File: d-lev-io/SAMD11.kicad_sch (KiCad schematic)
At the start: 30 parts, among them J6 PROG_HDR, SW1 SW_Push, SW2 SW_Push, SW3 SW_Push, U3 ATSAMD11D14A-M

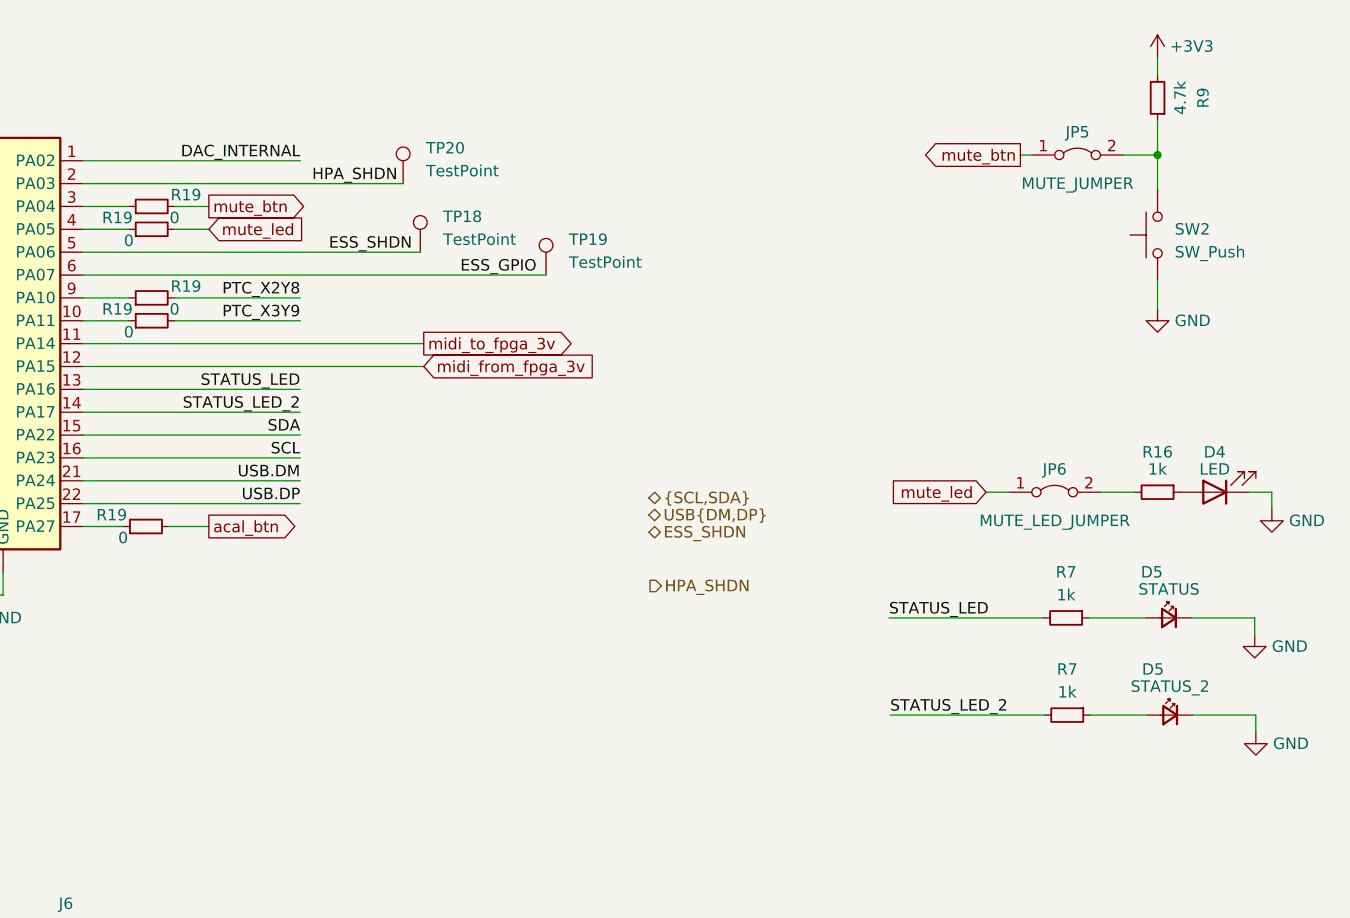
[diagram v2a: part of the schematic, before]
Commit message: io board more analog schematic capture
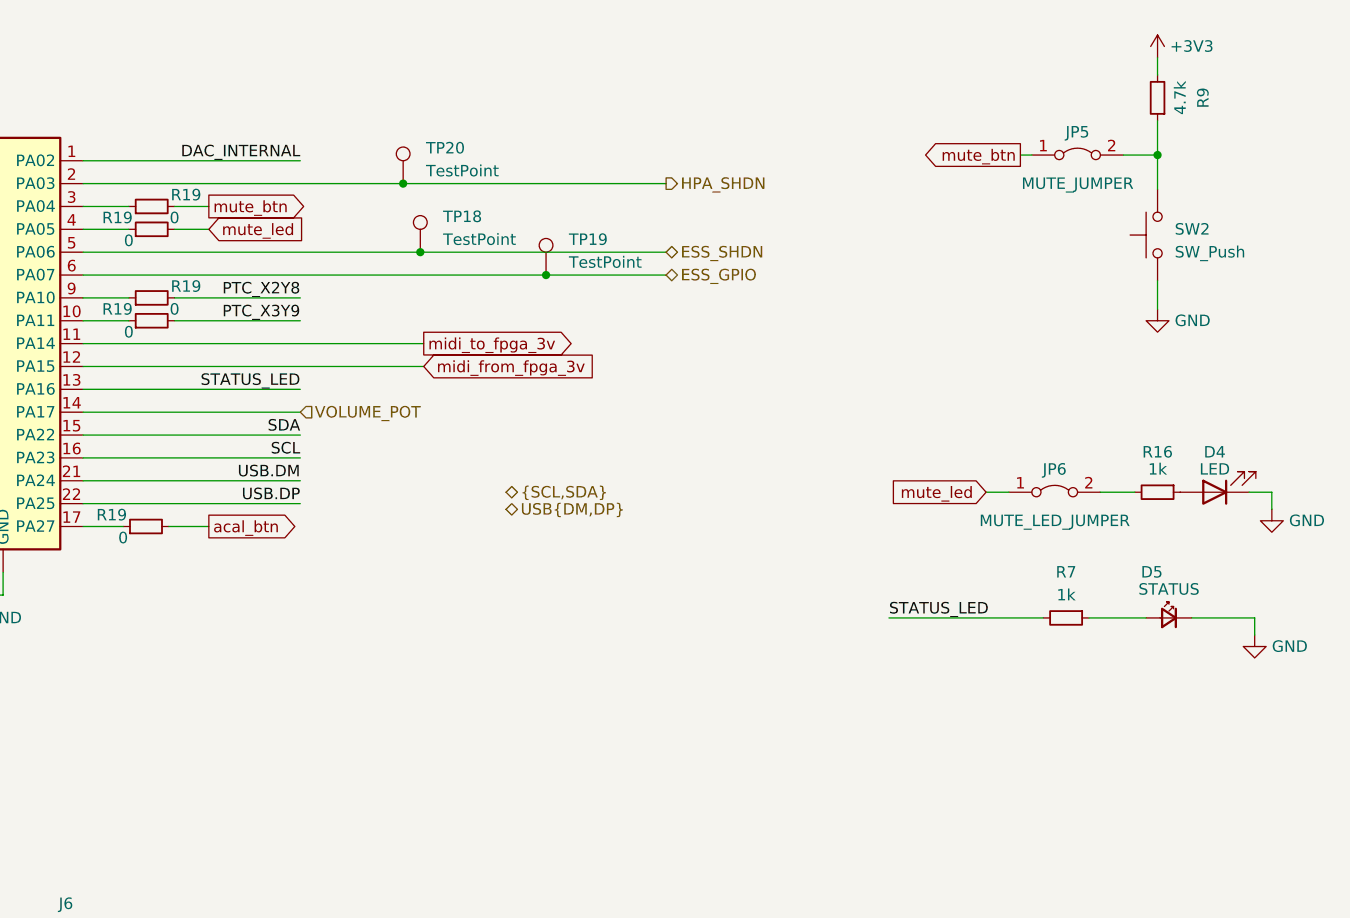
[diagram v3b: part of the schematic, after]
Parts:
- removed D5: STATUS_2, LED_SMD:LED_0603_1608Metric, symbol Device:LED_Small
- removed R7: 1k, Resistor_SMD:R_0603_1608Metric, symbol Device:R_Small
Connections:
- net STATUS_LED_2 renamed VOLUME_POT
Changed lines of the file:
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@@
 (kicad_sch (version 20230121) (generator eeschema)
   (paper "A4")
+  (junction (at 177.8 88.9) (diameter 0) (color 0 0 0 0)
+  )
   (junction (at 261.62 85.725) (diameter 0) (color 0 0 0 0)
   )
@@
   (junction (at 261.62 44.45) (diameter 0) (color 0 0 0 0)
   )
+  (junction (at 179.705 96.52) (diameter 0) (color 0 0 0 0)
+  )
   (junction (at 50.165 153.67) (diameter 0) (color 0 0 0 0)
   )
   (junction (at 49.53 88.9) (diameter 0) (color 0 0 0 0)
+  )
+  (junction (at 193.675 99.06) (diameter 0) (color 0 0 0 0)
   )
   (junction (at 50.165 131.445) (diameter 0) (color 0 0 0 0)
@@
     (stroke (width 0) (type default))
   )
-  (wire (pts (xy 272.542 149.86) (xy 272.542 147.955))
-    (stroke (width 0) (type default))
-  )
   (wire (pts (xy 99.695 89.535) (xy 99.695 88.9))
     (stroke (width 0) (type default))
@@
     (stroke (width 0) (type default))
   )
+  (wire (pts (xy 207.01 96.52) (xy 179.705 96.52))
+    (stroke (width 0) (type default))
+  )
   (wire (pts (xy 47.244 96.52) (xy 47.244 99.06))
     (stroke (width 0) (type default))
@@
     (stroke (width 0) (type default))
   )
-  (wire (pts (xy 231.902 147.955) (xy 249.047 147.955))
-    (stroke (width 0) (type default))
-  )
   (wire (pts (xy 47.244 99.06) (xy 59.69 99.06))
     (stroke (width 0) (type default))
@@
     (stroke (width 0) (type default))
   )
-  (wire (pts (xy 265.557 147.955) (xy 272.542 147.955))
-    (stroke (width 0) (type default))
-  )
   (wire (pts (xy 50.165 139.7) (xy 50.165 140.97))
     (stroke (width 0) (type default))
@@
     (stroke (width 0) (type default))
   )
+  (wire (pts (xy 207.01 99.06) (xy 193.675 99.06))
+    (stroke (width 0) (type default))
+  )
   (wire (pts (xy 61.595 131.445) (xy 61.595 139.065))
     (stroke (width 0) (type default))
@@
     (stroke (width 0) (type default))
   )
+  (wire (pts (xy 177.8 88.9) (xy 207.01 88.9))
+    (stroke (width 0) (type default))
+  )
   (wire (pts (xy 231.775 137.16) (xy 248.92 137.16))
     (stroke (width 0) (type default))
@@
   )
   (wire (pts (xy 142.24 124.46) (xy 166.37 124.46))
-    (stroke (width 0) (type default))
-  )
-  (wire (pts (xy 260.477 147.955) (xy 254.127 147.955))
     (stroke (width 0) (type default))
   )
@@
     (effects (font (size 1.27 1.27)) (justify left bottom))
   )
-  (label "STATUS_LED_2" (at 166.37 114.3 180) (fields_autoplaced)
-    (effects (font (size 1.27 1.27)) (justify right bottom))
-  )
   (label "SCL" (at 166.37 119.38 180) (fields_autoplaced)
     (effects (font (size 1.27 1.27)) (justify right bottom))
@@
     (effects (font (size 1.27 1.27)) (justify right bottom))
   )
-  (label "STATUS_LED_2" (at 231.902 147.955 0) (fields_autoplaced)
-    (effects (font (size 1.27 1.27)) (justify left bottom))
-  )
   (label "SDA" (at 59.69 96.52 180) (fields_autoplaced)
     (effects (font (size 1.27 1.27)) (justify right bottom))
@@
     (effects (font (size 1.27 1.27)) (justify right bottom))
   )
-  (label "ESS_GPIO" (at 184.15 99.06 0) (fields_autoplaced)
-    (effects (font (size 1.27 1.27)) (justify left bottom))
-  )
   (label "STATUS_LED" (at 166.37 111.76 180) (fields_autoplaced)
     (effects (font (size 1.27 1.27)) (justify right bottom))
@@
   )
   (label "DAC_INTERNAL" (at 166.37 86.36 180) (fields_autoplaced)
-    (effects (font (size 1.27 1.27)) (justify right bottom))
-  )
-  (label "ESS_SHDN" (at 169.545 96.52 0) (fields_autoplaced)
-    (effects (font (size 1.27 1.27)) (justify left bottom))
-  )
-  (label "HPA_SHDN" (at 177.165 88.9 180) (fields_autoplaced)
     (effects (font (size 1.27 1.27)) (justify right bottom))
   )
@@
     )
   )
-  (hierarchical_label "ESS_SHDN" (shape bidirectional) (at 205.105 127.635 0) (fields_autoplaced)
+  (hierarchical_label "ESS_GPIO" (shape bidirectional) (at 207.01 99.06 0) (fields_autoplaced)
     (effects (font (size 1.27 1.27)) (justify left))
   )
-  (hierarchical_label "USB{DM,DP}" (shape bidirectional) (at 205.105 125.73 0) (fields_autoplaced)
+  (hierarchical_label "ESS_SHDN" (shape bidirectional) (at 207.01 96.52 0) (fields_autoplaced)
     (effects (font (size 1.27 1.27)) (justify left))
   )
-  (hierarchical_label "HPA_SHDN" (shape output) (at 205.232 133.604 0) (fields_autoplaced)
+  (hierarchical_label "USB{DM,DP}" (shape bidirectional) (at 189.23 125.095 0) (fields_autoplaced)
     (effects (font (size 1.27 1.27)) (justify left))
   )
-  (hierarchical_label "{SCL,SDA}" (shape bidirectional) (at 205.105 123.825 0) (fields_autoplaced)
+  (hierarchical_label "VOLUME_POT" (shape input) (at 166.37 114.3 0) (fields_autoplaced)
     (effects (font (size 1.27 1.27)) (justify left))
   )
+  (hierarchical_label "HPA_SHDN" (shape output) (at 207.01 88.9 0) (fields_autoplaced)
+    (effects (font (size 1.27 1.27)) (justify left))
+  )
+  (hierarchical_label "{SCL,SDA}" (shape bidirectional) (at 189.23 123.19 0) (fields_autoplaced)
+    (effects (font (size 1.27 1.27)) (justify left))
+  )
   (symbol (lib_id "Device:R_Small") (at 47.244 93.98 180) (unit 1)
     (in_bom yes) (on_board yes) (dnp no)
@@
         (path "/9261a07b-ae4a-4d72-8042-ea097cd0e5ed/fd6a6c10-f456-4937-8c5d-f097bbb805c0"
           (reference "R20") (unit 1)
-        )
-      )
-    )
-  )
-  (symbol (lib_id "power:GND") (at 272.542 149.86 0) (unit 1)
-    (in_bom yes) (on_board yes) (dnp no) (fields_autoplaced)
-    (property "Reference" "#PWR023" (at 272.542 156.21 0)
-      (effects (font (size 1.27 1.27)) hide)
-    )
-    (property "Value" "GND" (at 274.447 151.1299 0)
-      (effects (font (size 1.27 1.27)) (justify left))
-    )
-    (property "Footprint" "" (at 272.542 149.86 0)
-      (effects (font (size 1.27 1.27)) hide)
-    )
-    (property "Datasheet" "" (at 272.542 149.86 0)
-      (effects (font (size 1.27 1.27)) hide)
-    )
-    (pin "1")
-    (instances
-      (project "d-lev-io"
-        (path "/9261a07b-ae4a-4d72-8042-ea097cd0e5ed"
-          (reference "#PWR023") (unit 1)
-        )
-        (path "/9261a07b-ae4a-4d72-8042-ea097cd0e5ed/fd6a6c10-f456-4937-8c5d-f097bbb805c0"
-          (reference "#PWR042") (unit 1)
-        )
-      )
-      (project "dlev-mini"
-        (path "/eb5e8bfd-9871-4528-bf57-58851bf63907/6062d07e-a4ed-44ac-a6b0-014aac464169"
-          (reference "#PWR0139") (unit 1)
         )
       )
@@
     )
   )
-  (symbol (lib_id "Device:R_Small") (at 251.587 147.955 270) (unit 1)
-    (in_bom yes) (on_board yes) (dnp no) (fields_autoplaced)
-    (property "Reference" "R7" (at 251.587 142.875 90)
-      (effects (font (size 1.27 1.27)))
-    )
-    (property "Value" "1k" (at 251.587 145.415 90)
-      (effects (font (size 1.27 1.27)))
-    )
-    (property "Footprint" "Resistor_SMD:R_0603_1608Metric" (at 251.587 147.955 0)
-      (effects (font (size 1.27 1.27)) hide)
-    )
-    (property "Datasheet" "~" (at 251.587 147.955 0)
-      (effects (font (size 1.27 1.27)) hide)
-    )
-    (pin "1")
-    (pin "2")
-    (instances
-      (project "d-lev-io"
-        (path "/9261a07b-ae4a-4d72-8042-ea097cd0e5ed"
-          (reference "R7") (unit 1)
-        )
-        (path "/9261a07b-ae4a-4d72-8042-ea097cd0e5ed/fd6a6c10-f456-4937-8c5d-f097bbb805c0"
-          (reference "R28") (unit 1)
-        )
-      )
-    )
-  )
   (symbol (lib_id "Switch:SW_Push") (at 50.165 146.05 90) (unit 1)
     (in_bom yes) (on_board yes) (dnp no)
@@
         )
       )
-    )
-  )
-  (symbol (lib_id "Device:LED_Small") (at 263.017 147.955 0) (mirror y) (unit 1)
-    (in_bom yes) (on_board yes) (dnp no)
-    (property "Reference" "D5" (at 261.112 142.875 0)
-      (effects (font (size 1.27 1.27)))
-    )
-    (property "Value" "STATUS_2" (at 263.017 144.78 0)
-      (effects (font (size 1.27 1.27)))
-    )
-    (property "Footprint" "LED_SMD:LED_0603_1608Metric" (at 263.017 147.955 90)
-      (effects (font (size 1.27 1.27)) hide)
-    )
-    (property "Datasheet" "~" (at 263.017 147.955 90)
-      (effects (font (size 1.27 1.27)) hide)
-    )
-    (pin "1")
-    (pin "2")
-    (instances
-      (project "d-lev-io"
-        (path "/9261a07b-ae4a-4d72-8042-ea097cd0e5ed"
-          (reference "D5") (unit 1)
-        )
-        (path "/9261a07b-ae4a-4d72-8042-ea097cd0e5ed/fd6a6c10-f456-4937-8c5d-f097bbb805c0"
-          (reference "D5") (unit 1)
-        )
-      )

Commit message: assign vol pot to analog pin
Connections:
- net ESS_GPIO: now also U3.14 (PA17); no longer U3.6 (PA07)
- net VOLUME_POT: now also U3.6 (PA07); no longer U3.14 (PA17)
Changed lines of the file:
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@@
   (junction (at 49.53 88.9) (diameter 0) (color 0 0 0 0)
   )
-  (junction (at 193.675 99.06) (diameter 0) (color 0 0 0 0)
+  (junction (at 206.121 114.3) (diameter 0) (color 0 0 0 0)
   )
   (junction (at 50.165 131.445) (diameter 0) (color 0 0 0 0)
@@
     (stroke (width 0) (type default))
   )
-  (wire (pts (xy 142.24 114.3) (xy 166.37 114.3))
+  (wire (pts (xy 142.24 114.3) (xy 206.121 114.3))
     (stroke (width 0) (type default))
   )
@@
     (stroke (width 0) (type default))
   )
-  (wire (pts (xy 142.24 99.06) (xy 193.675 99.06))
-    (stroke (width 0) (type default))
-  )
   (wire (pts (xy 142.24 88.9) (xy 177.8 88.9))
     (stroke (width 0) (type default))
@@
     (stroke (width 0) (type default))
   )
+  (wire (pts (xy 219.456 114.3) (xy 206.121 114.3))
+    (stroke (width 0) (type default))
+  )
   (wire (pts (xy 103.505 99.06) (xy 116.84 99.06))
     (stroke (width 0) (type default))
@@
     (stroke (width 0) (type default))
   )
-  (wire (pts (xy 207.01 99.06) (xy 193.675 99.06))
-    (stroke (width 0) (type default))
-  )
   (wire (pts (xy 61.595 131.445) (xy 61.595 139.065))
     (stroke (width 0) (type default))
   )
   (wire (pts (xy 146.685 179.07) (xy 158.75 179.07))
+    (stroke (width 0) (type default))
+  )
+  (wire (pts (xy 207.01 99.06) (xy 142.24 99.06))
     (stroke (width 0) (type default))
   )
@@
     )
   )
-  (hierarchical_label "ESS_GPIO" (shape bidirectional) (at 207.01 99.06 0) (fields_autoplaced)
-    (effects (font (size 1.27 1.27)) (justify left))
-  )
   (hierarchical_label "ESS_SHDN" (shape bidirectional) (at 207.01 96.52 0) (fields_autoplaced)
     (effects (font (size 1.27 1.27)) (justify left))
@@
     (effects (font (size 1.27 1.27)) (justify left))
   )
-  (hierarchical_label "VOLUME_POT" (shape input) (at 166.37 114.3 0) (fields_autoplaced)
+  (hierarchical_label "VOLUME_POT" (shape input) (at 207.01 99.06 0) (fields_autoplaced)
+    (effects (font (size 1.27 1.27)) (justify left))
+  )
+  (hierarchical_label "ESS_GPIO" (shape bidirectional) (at 219.456 114.3 0) (fields_autoplaced)
     (effects (font (size 1.27 1.27)) (justify left))
   )
@@
     )
   )
+  (symbol (lib_id "Connector:TestPoint") (at 206.121 114.3 0) (unit 1)
+    (in_bom yes) (on_board yes) (dnp no) (fields_autoplaced)
+    (property "Reference" "TP19" (at 208.661 110.363 0)
+      (effects (font (size 1.27 1.27)) (justify left))
+    )
+    (property "Value" "TestPoint" (at 208.661 112.903 0)
+      (effects (font (size 1.27 1.27)) (justify left))
+    )
+    (property "Footprint" "TestPoint:TestPoint_Pad_D1.5mm" (at 211.201 114.3 0)
+      (effects (font (size 1.27 1.27)) hide)
+    )
+    (property "Datasheet" "~" (at 211.201 114.3 0)
+      (effects (font (size 1.27 1.27)) hide)
+    )
+    (pin "1")
+    (instances
+      (project "d-lev-io"
+        (path "/9261a07b-ae4a-4d72-8042-ea097cd0e5ed/fd6a6c10-f456-4937-8c5d-f097bbb805c0"
+          (reference "TP19") (unit 1)
+        )
+      )
+    )
+  )
   (symbol (lib_id "Device:R_Small") (at 261.62 123.19 270) (unit 1)
     (in_bom yes) (on_board yes) (dnp no)
@@
         )
       )
-    )
-  )
-  (symbol (lib_id "Connector:TestPoint") (at 193.675 99.06 0) (unit 1)
-    (in_bom yes) (on_board yes) (dnp no) (fields_autoplaced)
-    (property "Reference" "TP19" (at 196.215 95.123 0)
-      (effects (font (size 1.27 1.27)) (justify left))
-    )
-    (property "Value" "TestPoint" (at 196.215 97.663 0)
-      (effects (font (size 1.27 1.27)) (justify left))
-    )
-    (property "Footprint" "TestPoint:TestPoint_Pad_D1.5mm" (at 198.755 99.06 0)
-      (effects (font (size 1.27 1.27)) hide)
-    )
-    (property "Datasheet" "~" (at 198.755 99.06 0)
-      (effects (font (size 1.27 1.27)) hide)
-    )
-    (pin "1")
-    (instances
-      (project "d-lev-io"
-        (path "/9261a07b-ae4a-4d72-8042-ea097cd0e5ed/fd6a6c10-f456-4937-8c5d-f097bbb805c0"
-          (reference "TP19") (unit 1)
-        )
-      )
